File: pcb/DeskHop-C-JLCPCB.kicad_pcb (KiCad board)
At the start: 2 copper layers, 66.9 x 74.5 mm, 82 parts, among them J201 Debug, J202 Computer, J203 Power, J204 Device, J301 Debug, J302 Computer, J303 Power, J304 Device, Q201 USB Power Switch, Q301 USB Power Switch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

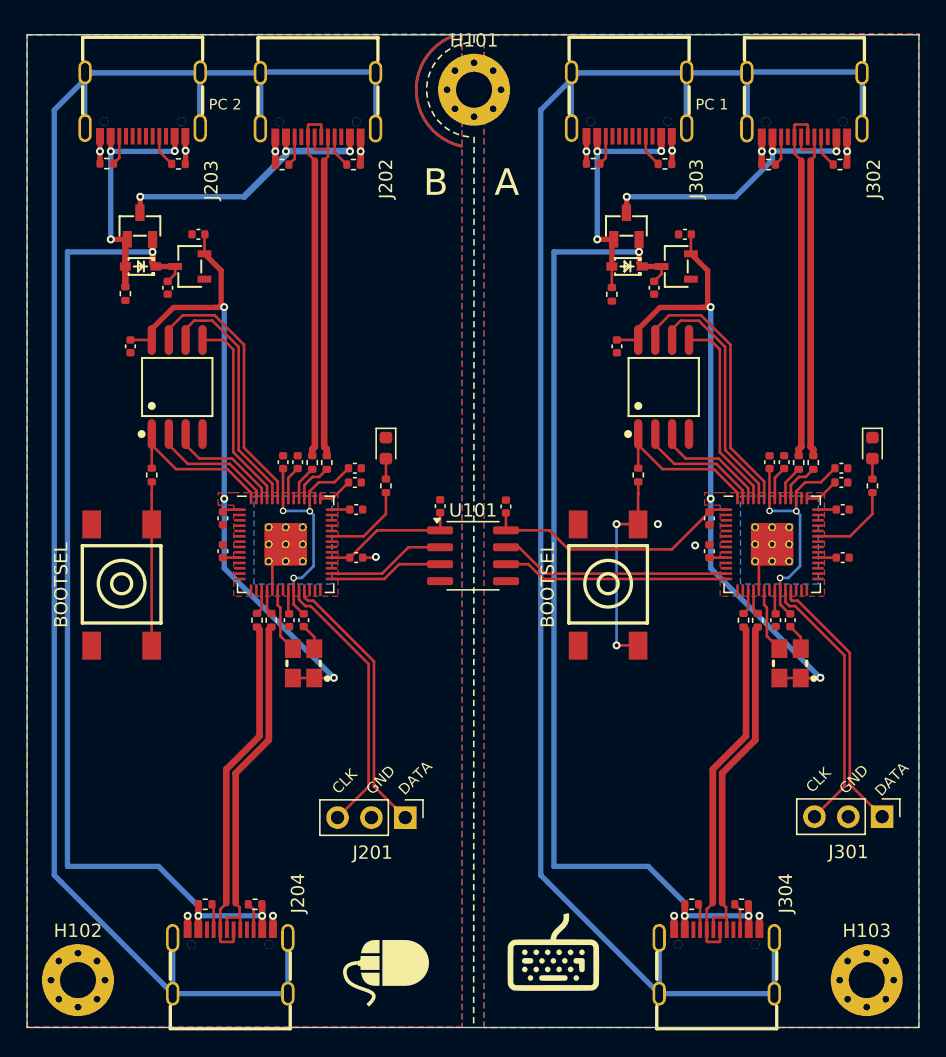
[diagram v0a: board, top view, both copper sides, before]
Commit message: Add test points for power supplies and oscillator.
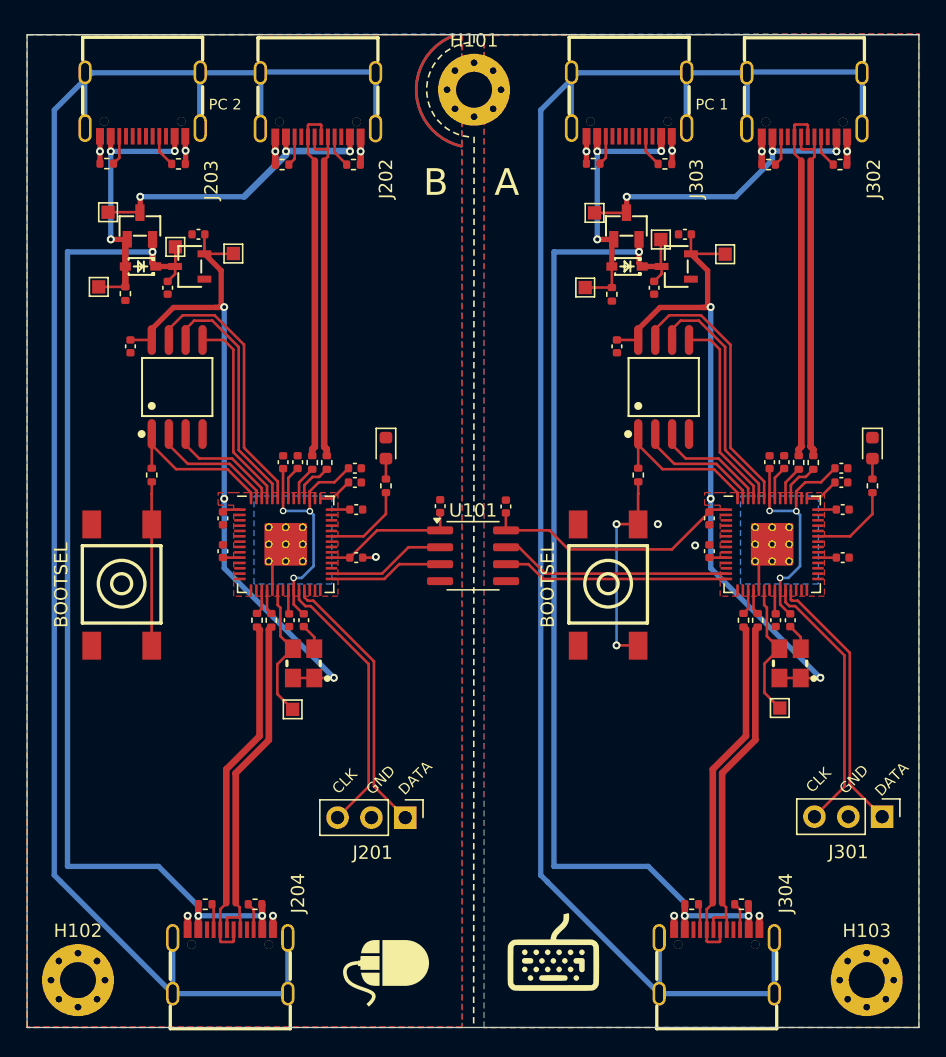
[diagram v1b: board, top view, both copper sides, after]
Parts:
- added TP201: TestPoint_Alt, TestPoint:TestPoint_Pad_1.0x1.0mm, F.Cu at (39.1, 60.0)
- added TP202: TestPoint_Alt, TestPoint:TestPoint_Pad_1.0x1.0mm, F.Cu at (39.9, 54.4)
- added TP203: TestPoint_Alt, TestPoint:TestPoint_Pad_1.0x1.0mm, F.Cu at (44.9, 57.0)
- added TP204: TestPoint_Alt, TestPoint:TestPoint_Pad_1.0x1.0mm, F.Cu at (49.2, 57.5)
- added TP205: TestPoint_Alt, TestPoint:TestPoint_Pad_1.0x1.0mm, F.Cu at (53.7, 91.7)
- added TP301: TestPoint_Alt, TestPoint:TestPoint_Pad_1.0x1.0mm, F.Cu at (75.7, 60.0)
- added TP302: TestPoint_Alt, TestPoint:TestPoint_Pad_1.0x1.0mm, F.Cu at (76.3, 54.5)
- added TP303: TestPoint_Alt, TestPoint:TestPoint_Pad_1.0x1.0mm, F.Cu at (81.3, 56.5)
- added TP304: TestPoint_Alt, TestPoint:TestPoint_Pad_1.0x1.0mm, F.Cu at (86.2, 57.5)
- added TP305: TestPoint_Alt, TestPoint:TestPoint_Pad_1.0x1.0mm, F.Cu at (90.2, 91.6)
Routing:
- net Net-(U203-XIN): track 4.87 -> 10.4 mm
- net Net-(U303-XIN): track 4.87 -> 10.3 mm
- net /Core Right (A)/3V3: track 80.0 -> 82.6 mm
- net /Core Left (B)/VUSB_COMP: track 20.7 -> 23.1 mm
- net /Core Right (A)/VUSB_COMP: track 20.7 -> 23.1 mm
- net /Core Left (B)/3V3: track 70.4 -> 72.5 mm
- net /Core Right (A)/VUSB: track 77.7 -> 79.7 mm
- net /Core Right (A)/VUSB_PWR: track 18.6 -> 20.6 mm
- net /Core Left (B)/VUSB_PWR: track 18.6 -> 20.6 mm
- net /Core Left (B)/VUSB: track 77.5 -> 79.0 mm

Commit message: Update schematic with MPN/LCSC, and update manual BOM.
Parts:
- C101, C102: value 100nf -> 100n

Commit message: First round of production cleanup.
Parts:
- moved TP203 2.52 mm to (44.9, 54.5)
- moved TP303 1.98 mm to (81.3, 54.5)
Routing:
- net /Core Left (B)/VUSB: track 79.0 -> 81.5 mm
- net /Core Right (A)/VUSB: track 79.7 -> 81.6 mm
- net /Core Right (A)/3V3: track 82.6 -> 81.2 mm
- net /Core Left (B)/3V3: track 72.5 -> 71.3 mm
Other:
- board text added: "DeskHop-C - USB-C Keyboard/Mouse Switch design by Hrvoje Cavrak, 12/2023 board by Kevin P. Fleming, 03/2024 https://github.com/hrvach License: GPL-3.0-only"
- board text removed: "DeskHop - Keyboard/Mouse Switch by Hrvoje Cavrak, 12/2023 https://github.com/hrvach"

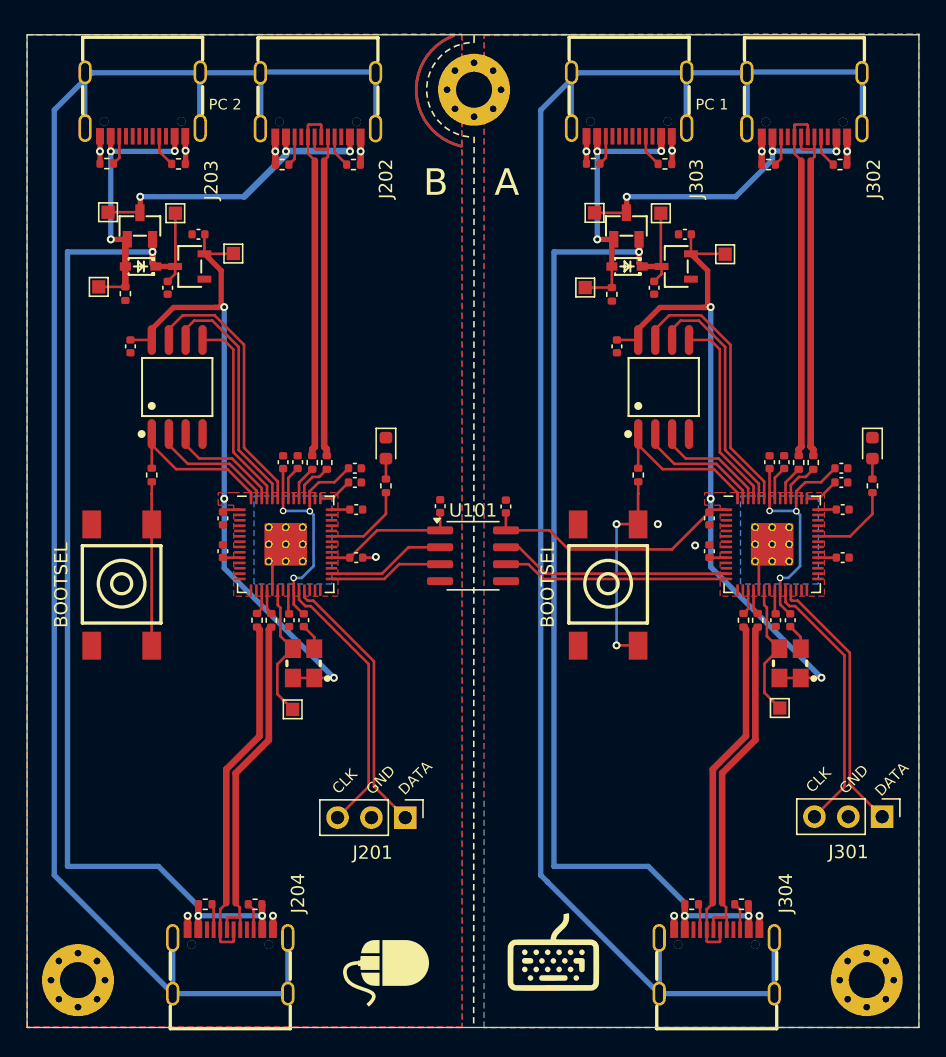
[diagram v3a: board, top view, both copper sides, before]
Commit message: Add decoupling caps for oscillators.
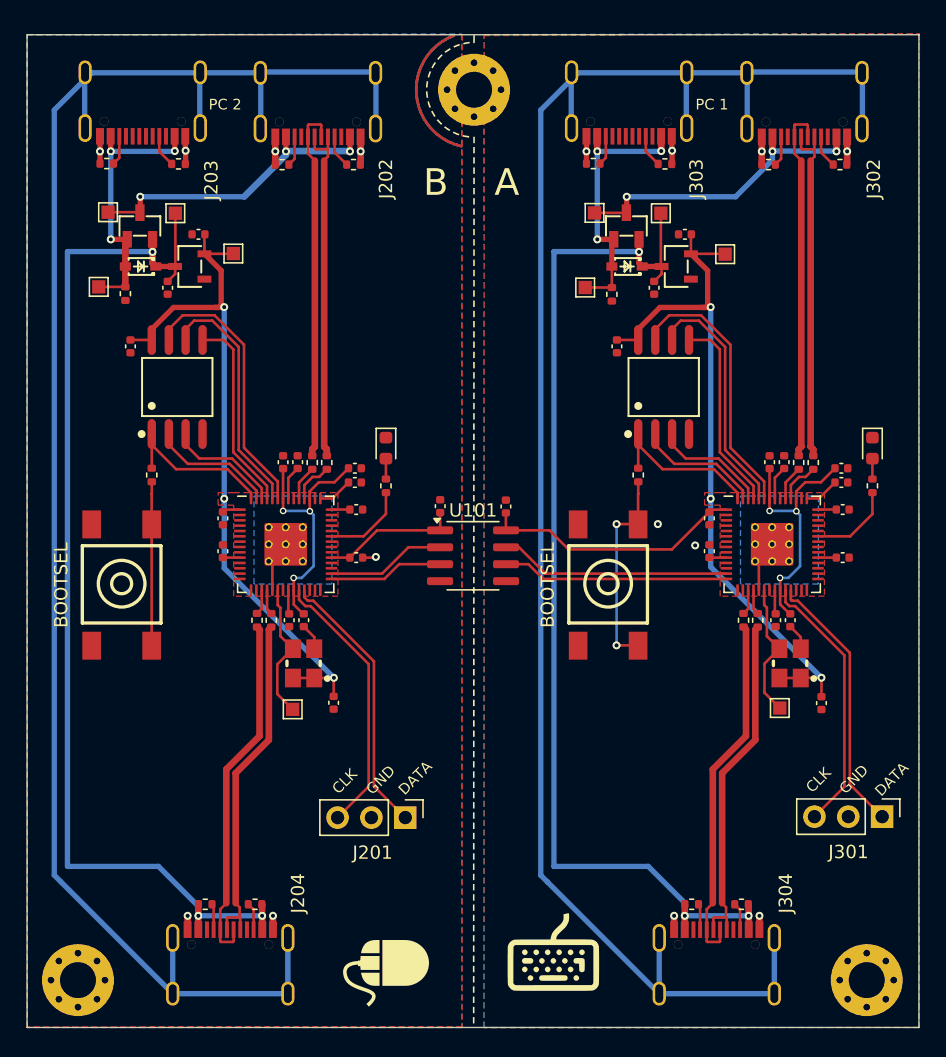
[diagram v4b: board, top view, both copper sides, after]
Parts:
- added C202: 100n, Capacitor_SMD:C_0402_1005Metric, F.Cu at (56.8, 91.2)
- added C302: 100n, Capacitor_SMD:C_0402_1005Metric, F.Cu at (93.4, 91.2)
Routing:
- net /Core Right (A)/3V3: track 81.2 -> 82.6 mm
- net /Core Left (B)/3V3: track 71.3 -> 72.7 mm

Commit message: More improvements:
* Used different GPIOs for the device USB so the traces can be kept
  away from the 12MHz oscillator circuit.

* Increased size of VBUS traces so that 1.5A@5V can be safely carried
  from the input connectors to the output connectors.

* Various minor tweaks.
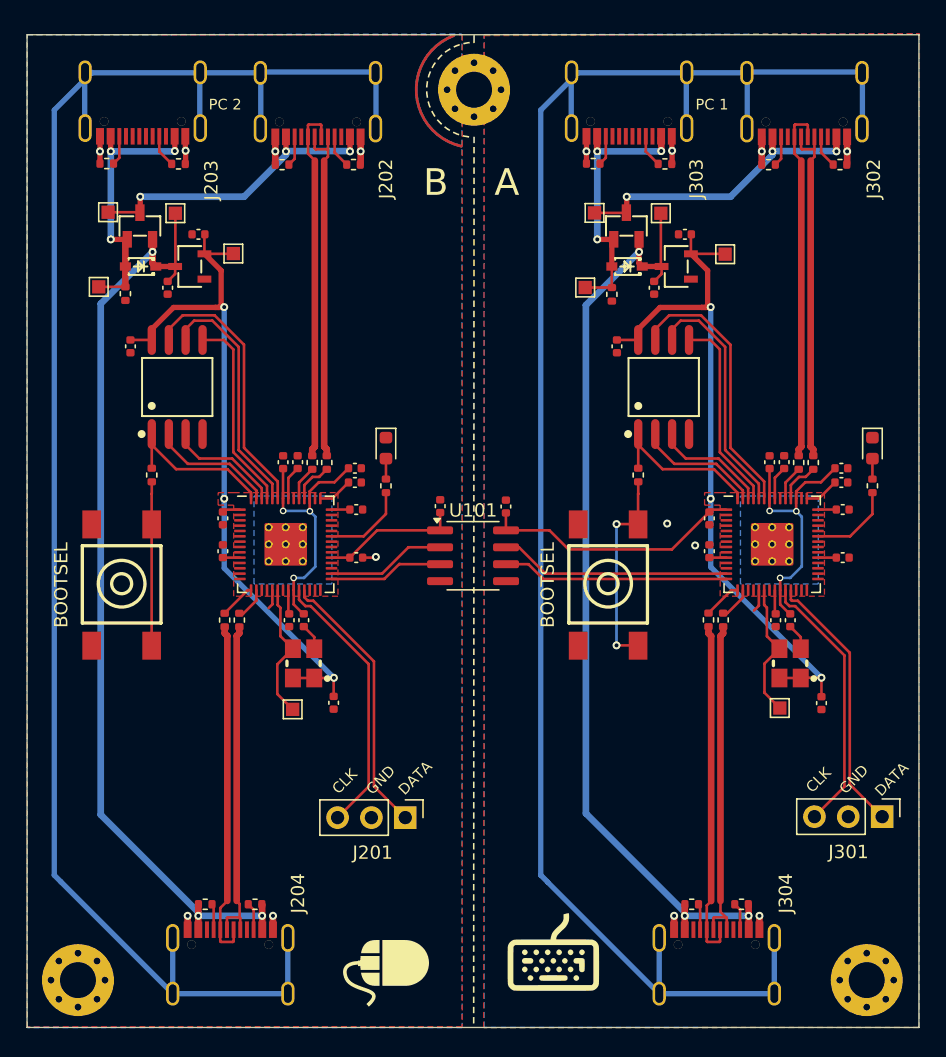
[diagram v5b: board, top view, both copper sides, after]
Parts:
- moved R306 2.63 mm to (84.9, 85.0)
- moved R305 2.60 mm to (86.0, 85.0)
- moved R206 2.43 mm to (48.6, 85.0)
- moved R205 2.40 mm to (49.7, 85.0)
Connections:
- R205 pad 2: Net-(U203-GPIO15) -> Net-(U203-GPIO13)
- R206 pad 2: Net-(U203-GPIO14) -> Net-(U203-GPIO12)
- R305 pad 2: Net-(U303-GPIO15) -> Net-(U303-GPIO13)
- R306 pad 2: Net-(U303-GPIO14) -> Net-(U303-GPIO12)
- U203 pad 15: unconnected-(U203-GPIO12-Pad15) -> Net-(U203-GPIO12)
- U203 pad 16: unconnected-(U203-GPIO13-Pad16) -> Net-(U203-GPIO13)
- U203 pad 17: Net-(U203-GPIO14) -> unconnected-(U203-GPIO14-Pad17)
- U203 pad 18: Net-(U203-GPIO15) -> unconnected-(U203-GPIO15-Pad18)
- U303 pad 15: unconnected-(U303-GPIO12-Pad15) -> Net-(U303-GPIO12)
- U303 pad 16: unconnected-(U303-GPIO13-Pad16) -> Net-(U303-GPIO13)
- U303 pad 17: Net-(U303-GPIO14) -> unconnected-(U303-GPIO14-Pad17)
- U303 pad 18: Net-(U303-GPIO15) -> unconnected-(U303-GPIO15-Pad18)
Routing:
- net /Core Right (A)/VUSB: track 81.7 -> 72.0 mm
- net /Core Left (B)/VUSB: track 81.6 -> 72.0 mm
- net Net-(U303-GPIO12): track 0.00 -> 2.89 mm
- net Net-(U203-GPIO12): track 0.00 -> 2.70 mm
- net Net-(U303-GPIO13): track 0.00 -> 2.53 mm
- net Net-(U203-GPIO13): track 0.00 -> 2.45 mm
- net Net-(U303-GPIO14): track 1.89 -> 0.00 mm
- net Net-(U203-GPIO14): track 1.89 -> 0.00 mm
- net Net-(U203-GPIO15): track 1.88 -> 0.00 mm
- net Net-(U303-GPIO15): track 1.88 -> 0.00 mm
- net /Core Right (A)/DEVICE USB-: track 26.8 -> 25.7 mm
- net /Core Left (B)/DEVICE USB+: track 25.8 -> 24.8 mm
- net /Core Left (B)/DEVICE USB-: track 26.8 -> 25.8 mm
- net /Core Right (A)/DEVICE USB+: track 25.8 -> 24.9 mm
- net /Core Left (B)/GND: track 15.6 -> 14.8 mm
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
